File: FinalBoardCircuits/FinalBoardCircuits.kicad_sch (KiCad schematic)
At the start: 1 part, among them J6 Conn_02x30_Odd_Even

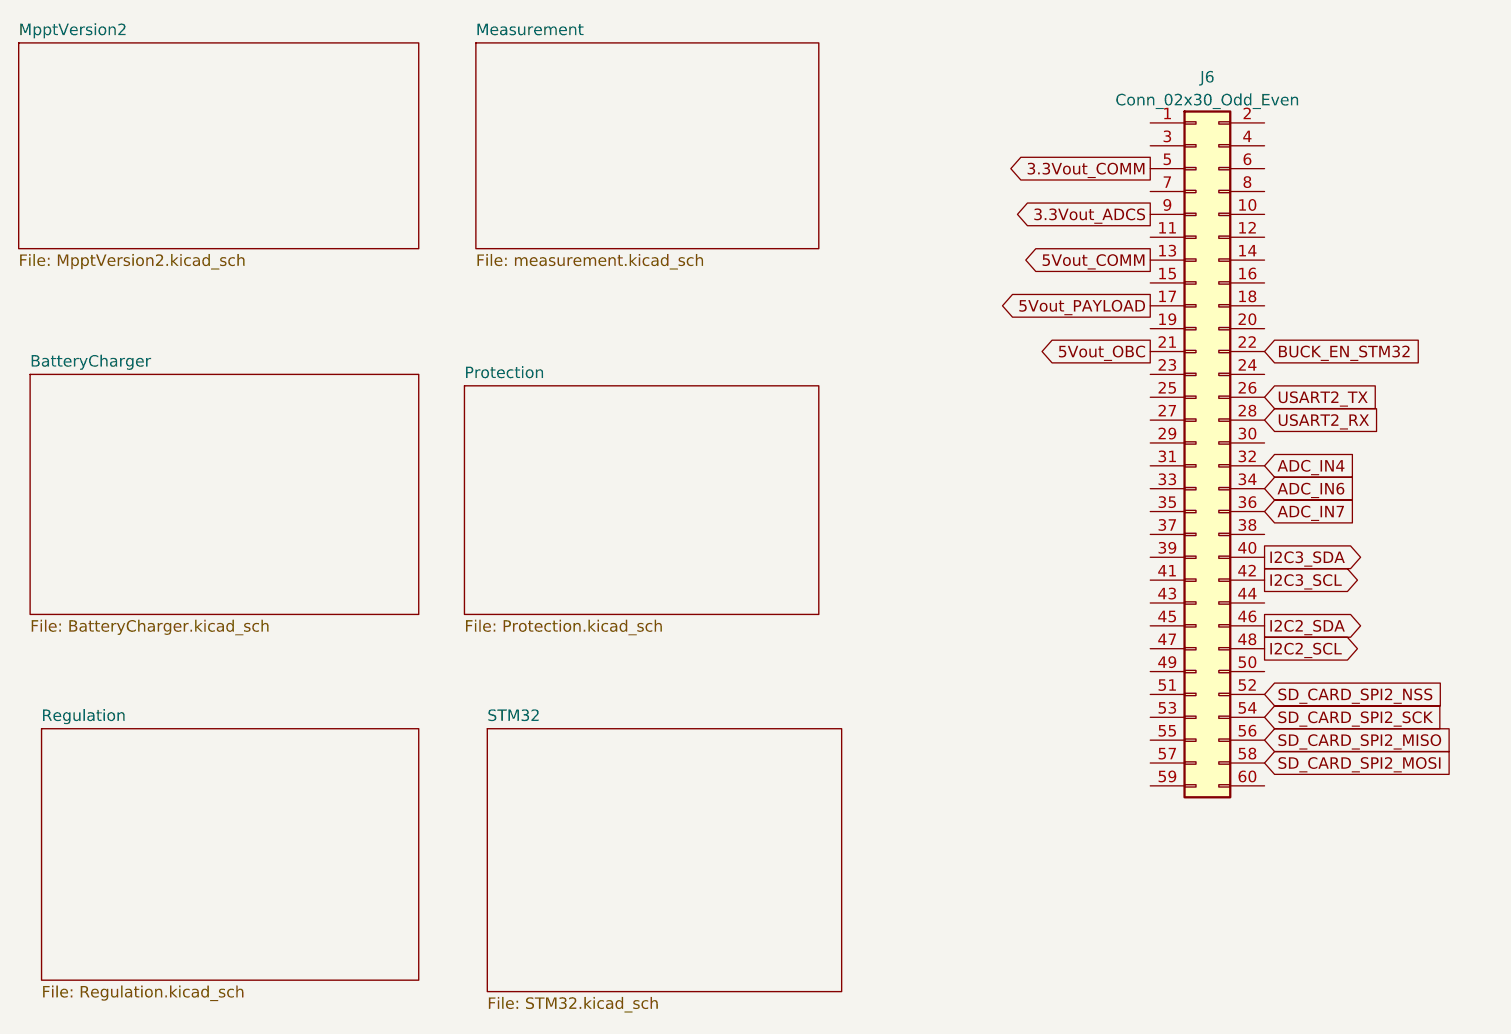
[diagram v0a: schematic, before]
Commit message: Added fuel guage
Added fuel guage circuit to the final design.
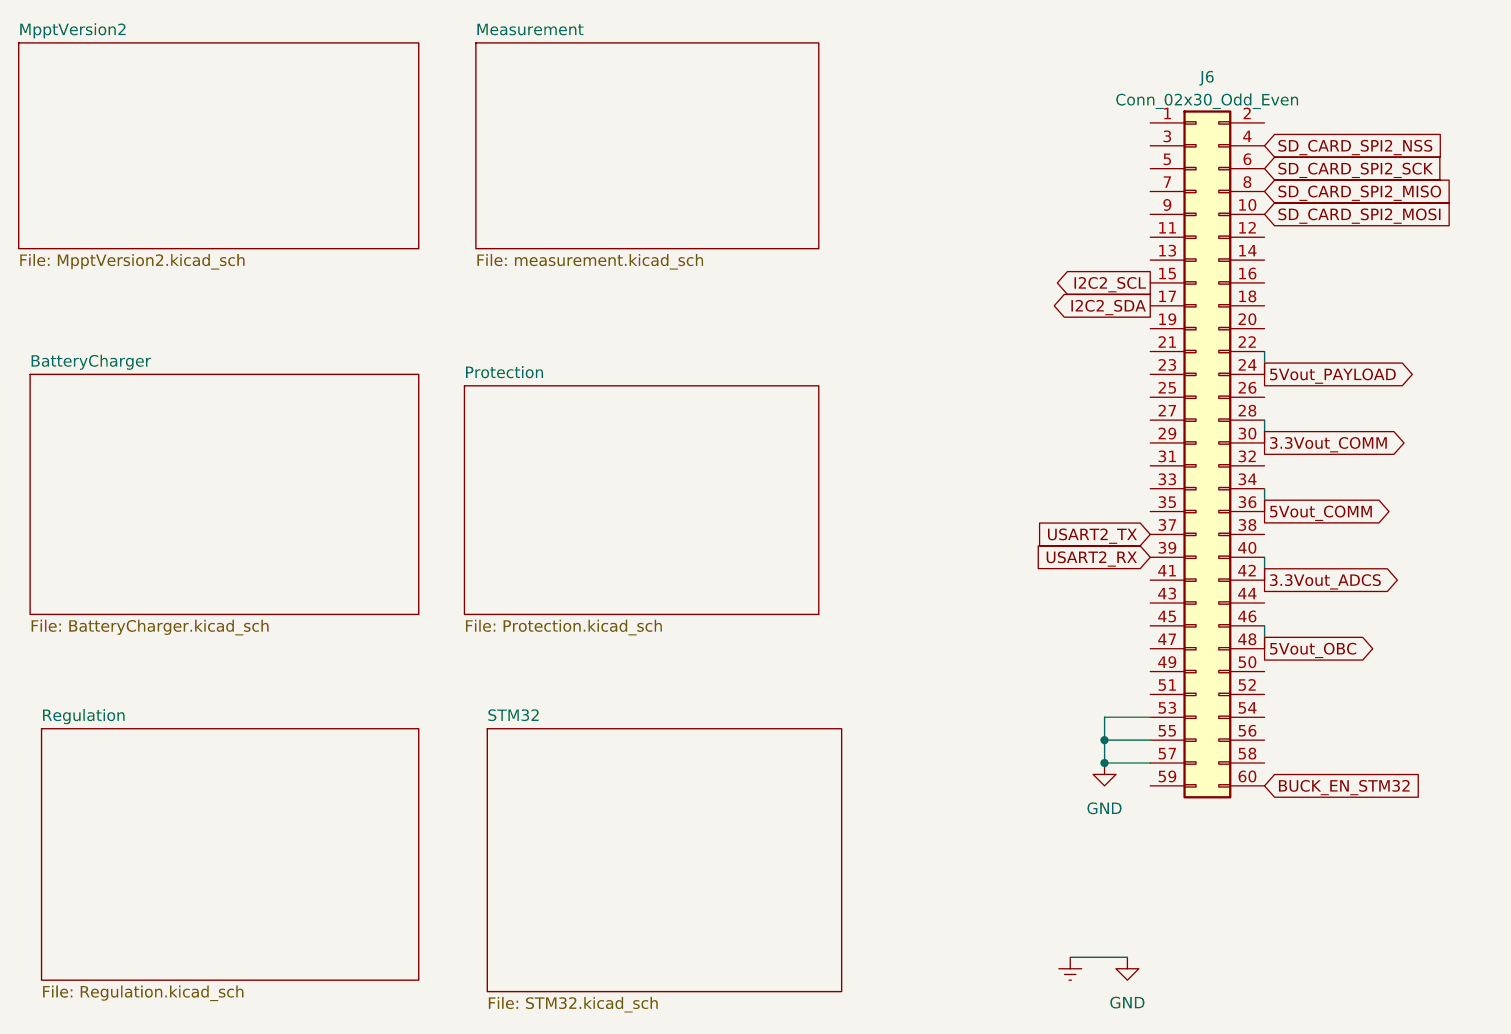
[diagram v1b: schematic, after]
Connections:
- net ADC_IN6 is gone; now on net 5Vout_COMM: J6.34 (Pin_34)
- net ADC_IN7 is gone; now on net 5Vout_COMM: J6.36 (Pin_36)
- net I2C3_SCL is gone; now on net 3.3Vout_ADCS: J6.42 (Pin_42)
- net I2C3_SDA is gone; now on net 3.3Vout_ADCS: J6.40 (Pin_40)
- net 3.3Vout_ADCS: no longer J6.9 (Pin_9)
- net 3.3Vout_COMM: now also J6.28 (Pin_28), J6.30 (Pin_30); no longer J6.5 (Pin_5)
- net 5Vout_COMM: no longer J6.13 (Pin_13)
- net 5Vout_OBC: now also J6.46 (Pin_46), J6.48 (Pin_48); no longer J6.21 (Pin_21)
- net 5Vout_PAYLOAD: now also J6.22 (Pin_22), J6.24 (Pin_24); no longer J6.17 (Pin_17)
- net BUCK_EN_STM32: now also J6.60 (Pin_60); no longer J6.22 (Pin_22)
- net I2C2_SCL: now also J6.15 (Pin_15); no longer J6.48 (Pin_48)
- net I2C2_SDA: now also J6.17 (Pin_17); no longer J6.46 (Pin_46)
- net SD_CARD_SPI2_MISO: now also J6.8 (Pin_8); no longer J6.56 (Pin_56)
- net SD_CARD_SPI2_MOSI: now also J6.10 (Pin_10); no longer J6.58 (Pin_58)
- net SD_CARD_SPI2_NSS: now also J6.4 (Pin_4); no longer J6.52 (Pin_52)
- net SD_CARD_SPI2_SCK: now also J6.6 (Pin_6); no longer J6.54 (Pin_54)
- net USART2_RX: now also J6.39 (Pin_39); no longer J6.28 (Pin_28)
- net USART2_TX: now also J6.37 (Pin_37); no longer J6.26 (Pin_26)
- net Earth: now reaches J6.53 (Pin_53)
- net Earth: now also J6.55 (Pin_55), J6.57 (Pin_57)
- net ADC_IN4: no longer names the net of J6.32 (Pin_32)
